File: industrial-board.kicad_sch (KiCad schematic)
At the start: 25 parts, among them J1 Conn_01x06_Pin, J2 Conn_01x14, J3 Conn_01x15, J4 Conn_01x04, J5 Conn_01x03, SW1 SW_Push, U1 STM32F103C8Tx, U2 AMS1117-3.3, U3 PEAK P6CU-2405ELF, U4 MAX3485, Y1 8MHz, Y2 32KHz

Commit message: change references
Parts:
- renumbered BT2 to BT1, C5 to C1, C6 to C2, C7 to C3, C8 to C4, C24 to C5, C3 to C6, J3 to J2, J5 to J3, J2 to J4, J4 to J5, R51 to R1, R7 to R2
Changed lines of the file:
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@@
 		(dnp no)
 		(fields_autoplaced yes)
-		(property "Reference" "C8"
+		(property "Reference" "C4"
 			(at 146.05 124.46 90)
 			(effects
@@
 			(project "escalator-board"
 				(path "/134c3394-7007-4a3f-89d9-4332a6c1de73"
-					(reference "C8")
+					(reference "C4")
 					(unit 1)
 				)
@@
 		(dnp no)
 		(fields_autoplaced yes)
-		(property "Reference" "J5"
+		(property "Reference" "J3"
 			(at 208.28 140.9699 0)
 			(effects
@@
 			(project ""
 				(path "/134c3394-7007-4a3f-89d9-4332a6c1de73"
-					(reference "J5")
+					(reference "J3")
 					(unit 1)
 				)
@@
 		(dnp no)
 		(fields_autoplaced yes)
-		(property "Reference" "J2"
+		(property "Reference" "J4"
 			(at 242.57 119.3799 0)
 			(effects
@@
 			(project ""
 				(path "/134c3394-7007-4a3f-89d9-4332a6c1de73"
-					(reference "J2")
+					(reference "J4")
 					(unit 1)
 				)
@@
 		(dnp no)
 		(fields_autoplaced yes)
-		(property "Reference" "C6"
+		(property "Reference" "C2"
 			(at 146.05 96.52 90)
 			(effects
@@
 			(project "escalator-board"
 				(path "/134c3394-7007-4a3f-89d9-4332a6c1de73"
-					(reference "C6")
+					(reference "C2")
 					(unit 1)
 				)
@@
 		(dnp no)
 		(fields_autoplaced yes)
-		(property "Reference" "J3"
+		(property "Reference" "J2"
 			(at 208.28 106.6799 0)
 			(effects
@@
 			(project "escalator-board"
 				(path "/134c3394-7007-4a3f-89d9-4332a6c1de73"
-					(reference "J3")
+					(reference "J2")
 					(unit 1)
 				)
@@
 		(dnp no)
 		(fields_autoplaced yes)
-		(property "Reference" "C5"
+		(property "Reference" "C1"
 			(at 146.05 82.55 90)
 			(effects
@@
 			(project "escalator-board"
 				(path "/134c3394-7007-4a3f-89d9-4332a6c1de73"
-					(reference "C5")
+					(reference "C1")
 					(unit 1)
 				)
@@
 		(dnp no)
 		(fields_autoplaced yes)
-		(property "Reference" "C24"
+		(property "Reference" "C5"
 			(at 43.18 111.7599 0)
 			(effects
@@
 			(project ""
 				(path "/134c3394-7007-4a3f-89d9-4332a6c1de73"
-					(reference "C24")
+					(reference "C5")
 					(unit 1)
 				)
@@
 		(dnp no)
 		(fields_autoplaced yes)
-		(property "Reference" "R7"
+		(property "Reference" "R2"
 			(at 245.11 50.7999 0)
 			(effects
@@
 			(project "escalator-board"
 				(path "/134c3394-7007-4a3f-89d9-4332a6c1de73"
-					(reference "R7")
+					(reference "R2")
 					(unit 1)
 				)
@@
 		(dnp no)
 		(fields_autoplaced yes)
-		(property "Reference" "C7"
+		(property "Reference" "C3"
 			(at 146.05 110.49 90)
 			(effects
@@
 			(project "escalator-board"
 				(path "/134c3394-7007-4a3f-89d9-4332a6c1de73"
-					(reference "C7")
+					(reference "C3")
 					(unit 1)
 				)
@@
 		(dnp no)
 		(fields_autoplaced yes)
-		(property "Reference" "BT2"
+		(property "Reference" "BT1"
 			(at 38.1 173.4184 0)
 			(effects
@@
 			(project "escalator-board"
 				(path "/134c3394-7007-4a3f-89d9-4332a6c1de73"
-					(reference "BT2")
+					(reference "BT1")
 					(unit 1)
 				)
@@
 		(dnp no)
 		(fields_autoplaced yes)
-		(property "Reference" "C3"
+		(property "Reference" "C6"
 			(at 96.52 147.3199 0)
 			(effects
@@
 			(project "escalator-board"
 				(path "/134c3394-7007-4a3f-89d9-4332a6c1de73"
-					(reference "C3")
+					(reference "C6")
 					(unit 1)
 				)
@@
 		(dnp no)
 		(fields_autoplaced yes)
-		(property "Reference" "J4"
+		(property "Reference" "J5"
 			(at 242.57 92.7099 0)
 			(effects
@@
 			(project ""
 				(path "/134c3394-7007-4a3f-89d9-4332a6c1de73"
-					(reference "J4")
+					(reference "J5")
 					(unit 1)
 				)
@@
 		(dnp no)
 		(fields_autoplaced yes)
-		(property "Reference" "R51"
+		(property "Reference" "R1"
 			(at 45.72 100.33 90)
 			(effects
@@
 			(project ""
 				(path "/134c3394-7007-4a3f-89d9-4332a6c1de73"
-					(reference "R51")
+					(reference "R1")
 					(unit 1)
 				)
@@
 		)
 		(instances
-			(project "escalator-board"
+			(project "industrial-board"
 				(path "/134c3394-7007-4a3f-89d9-4332a6c1de73"
 					(page "3")
@@
 		)
 		(instances
-			(project "escalator-board"
+			(project "industrial-board"
 				(path "/134c3394-7007-4a3f-89d9-4332a6c1de73"
 					(page "2")

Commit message: minor changes
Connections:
- net RS485+: now also J3.2 (Pin_2); no longer J3.1 (Pin_1)
- net RS485-: now also J3.1 (Pin_1); no longer J3.2 (Pin_2)
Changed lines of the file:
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@@
 		)
 	)
-	(label "RS485-"
+	(label "RS485+"
 		(at 198.12 142.24 180)
 		(fields_autoplaced yes)
@@
 		)
 	)
-	(label "RS485+"
+	(label "RS485-"
 		(at 198.12 139.7 180)
 		(fields_autoplaced yes)

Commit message: add C values
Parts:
- C5: value C -> 1uF
- C6: value C -> 10uF

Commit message: update project to kicad 9
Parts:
- H1, H2, H3, H4: footprint MountingHole:MountingHole_4.3mm_M4 -> MountingHole:MountingHole_3.2mm_M3

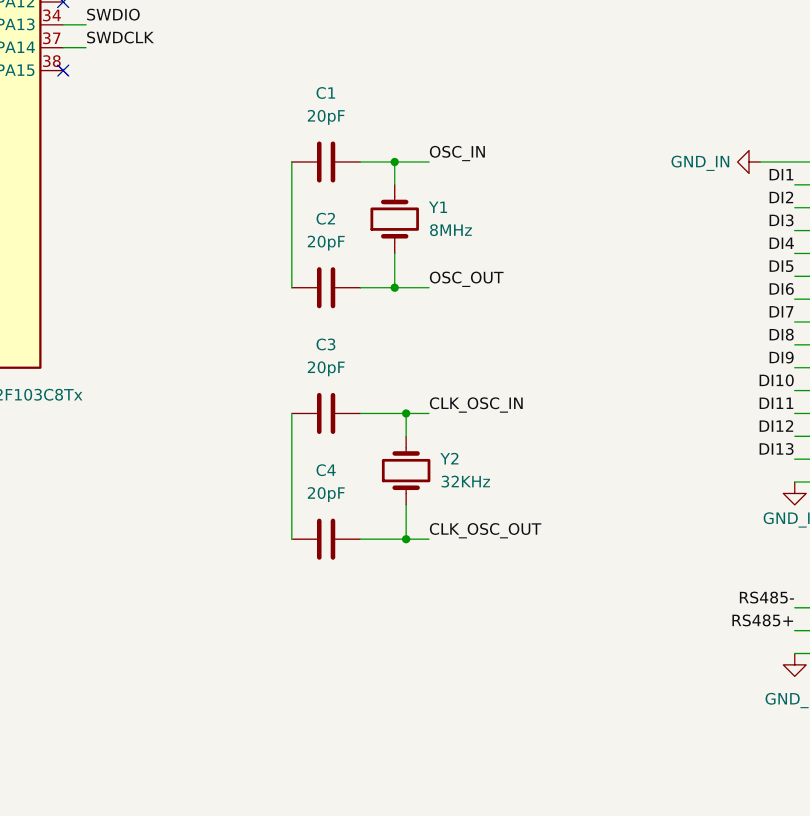
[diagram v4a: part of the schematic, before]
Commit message: ground crystal oscillators
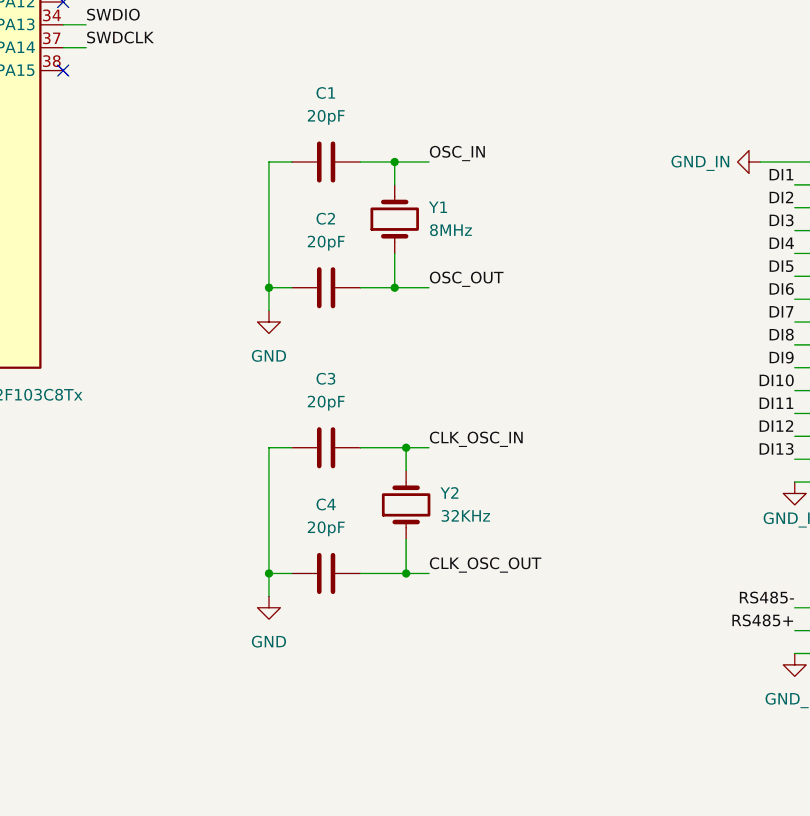
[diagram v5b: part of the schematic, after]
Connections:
- net GND: now also C1.1, C2.1, C3.1, C4.1
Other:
- moved on the sheet: C3, C4, Y2
